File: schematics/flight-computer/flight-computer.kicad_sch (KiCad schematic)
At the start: 45 parts, among them J1 BATT, J2 CHG, J3 SWD, J4 BLACKBOX, J5 USB C, J6 GPS, J7 TELEM, J9 Expansion Slot, U1 MAX14787E, U2 STM32F405RGT6, Y1 26M

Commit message: Rename to Lychee
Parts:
- C1, C10, C11, C12, C2, C3, C4, C5, C6, C7, C8, C9: footprint Strix:C_0402 -> Lychee:C_0402
- D1, D10, D11, D12, D13, D14, D2, D3, D4, D5, D6, D7, D8, D9: footprint Strix:D_0402 -> Lychee:D_0402
- H1, H2, H3, H4: footprint Strix:MountingHole_Pad -> Lychee:MountingHole_Pad
- J1: footprint Strix:Molex_Nano-Fit_105313-1103 -> Lychee:Molex_Nano-Fit_105313-1103
- J2: footprint Strix:Molex_Nano-Fit_105313-1102 -> Lychee:Molex_Nano-Fit_105313-1102
- J3: footprint Strix:Header_SWD -> Lychee:Header_SWD
- J4: footprint Strix:Molex_Nano-Fit_105314-1108 -> Lychee:Molex_Nano-Fit_105314-1108
- J5: footprint Strix:USB_C -> Lychee:USB_C
- J6, J7: footprint Strix:SMA-Edge -> Lychee:SMA-Edge
- J9: footprint Strix:Header_RaspberryPi -> Lychee:Header_RaspberryPi
- R1, R2, R3, R4: footprint Strix:R_0402 -> Lychee:R_0402
- U1: footprint Strix:MAX14787E -> Lychee:MAX14787E
- U2: footprint Strix:STM32F405RGT6 -> Lychee:STM32F405RGT6
- Y1: footprint Strix:Xtal-20x16 -> Lychee:Xtal-20x16
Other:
- title: HAB Flight Computer -> Lychee Flight Computer

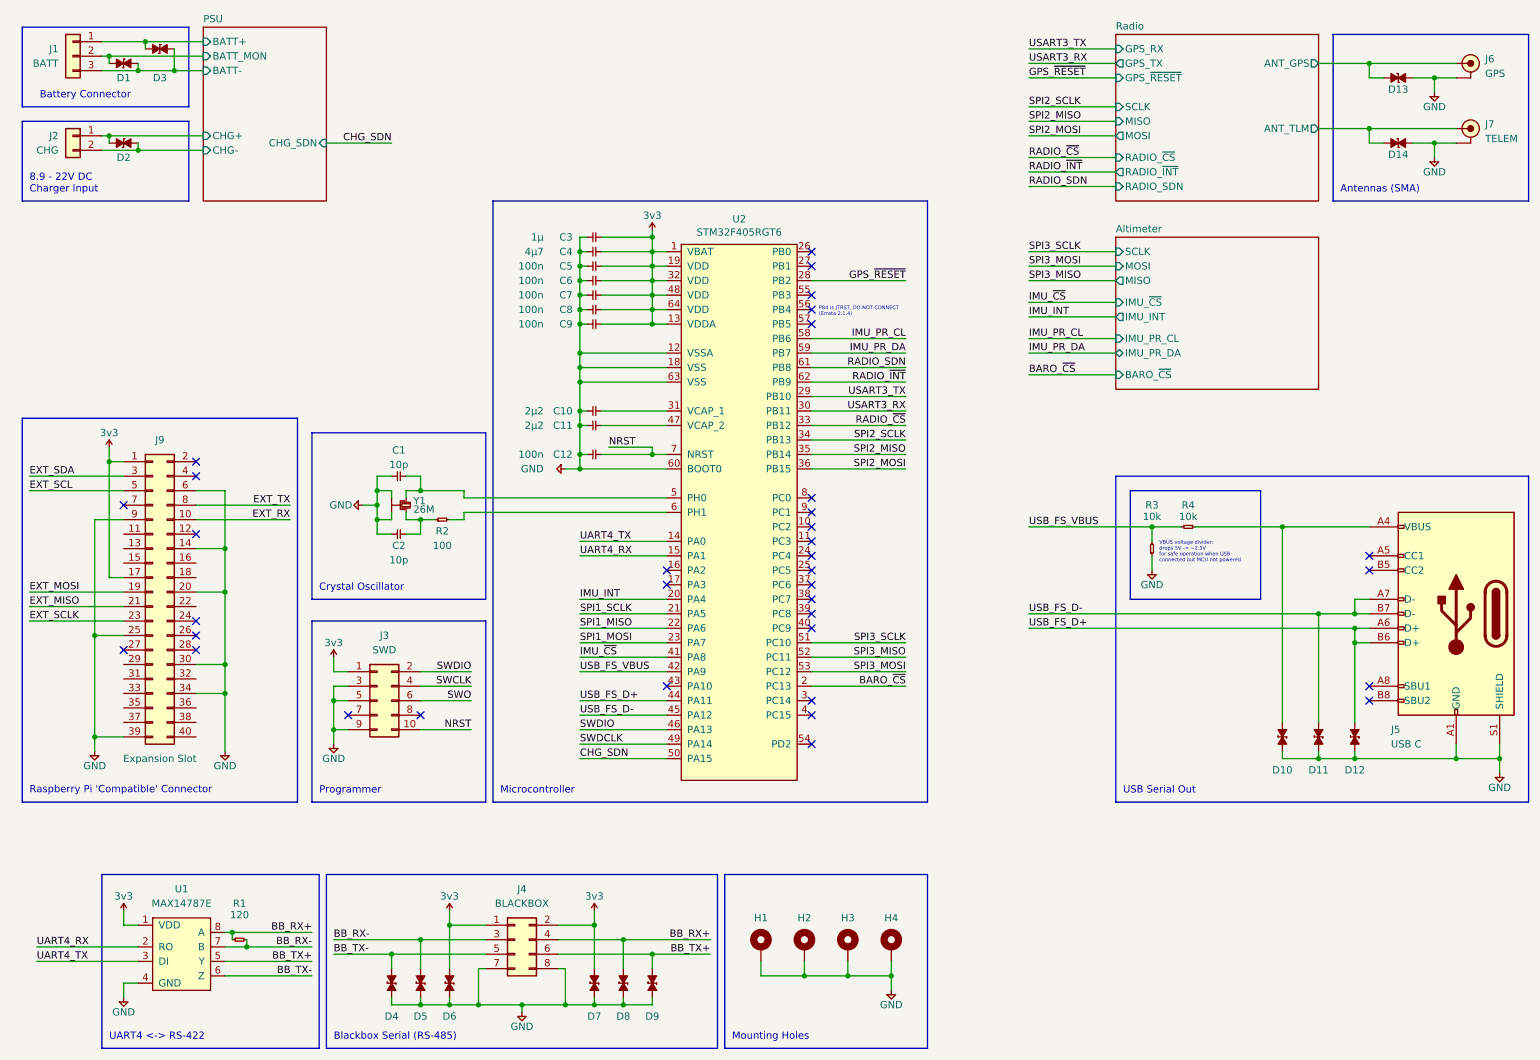
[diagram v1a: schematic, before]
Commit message: Migrate to common Strix lib via submodule
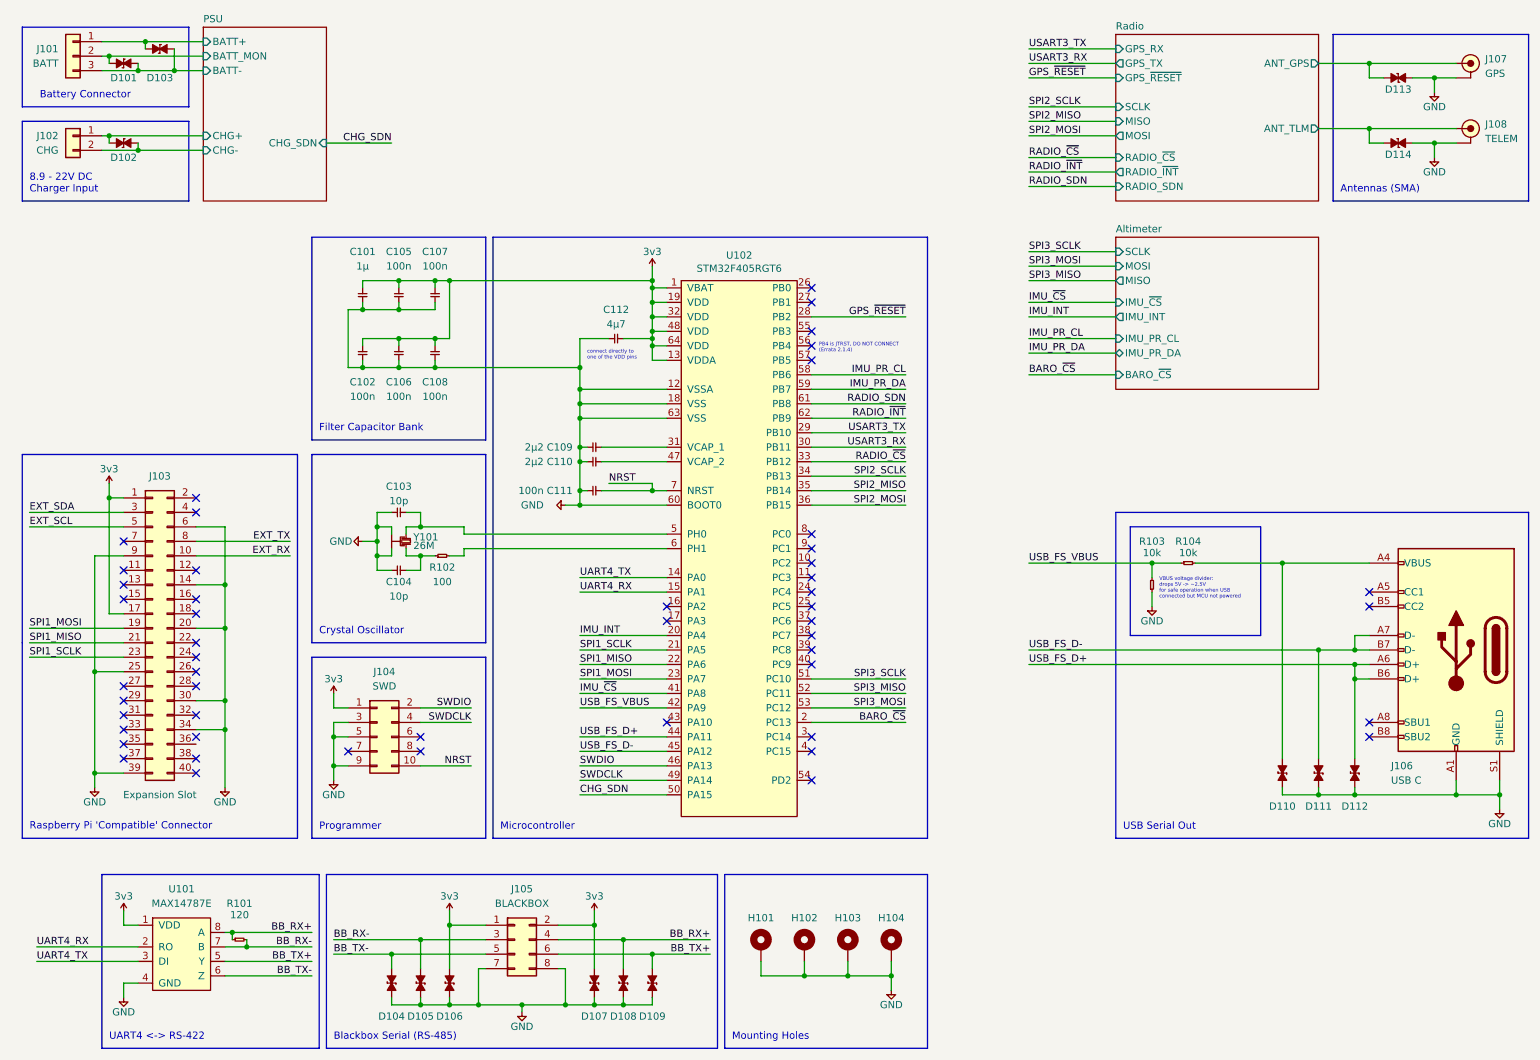
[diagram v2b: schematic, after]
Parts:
- C101: renamed from C3; footprint Lychee:C_0402 -> Strix:C_0402
- C102: renamed from C7; footprint Lychee:C_0402 -> Strix:C_0402
- C103: renamed from C1; footprint Lychee:C_0402 -> Strix:C_0402
- C104: renamed from C2; footprint Lychee:C_0402 -> Strix:C_0402
- C105: renamed from C5; footprint Lychee:C_0402 -> Strix:C_0402
- C106: renamed from C8; footprint Lychee:C_0402 -> Strix:C_0402
- C107: renamed from C6; footprint Lychee:C_0402 -> Strix:C_0402
- C108: renamed from C9; footprint Lychee:C_0402 -> Strix:C_0402
- C109: renamed from C10; footprint Lychee:C_0402 -> Strix:C_0402
- C110: renamed from C11; footprint Lychee:C_0402 -> Strix:C_0402
- C111: renamed from C12; footprint Lychee:C_0402 -> Strix:C_0402
- C112: renamed from C4; footprint Lychee:C_0402 -> Strix:C_0402
- D101: renamed from D1; footprint Lychee:D_0402 -> Strix:D_0402
- D102: renamed from D2; footprint Lychee:D_0402 -> Strix:D_0402
- D103: renamed from D3; footprint Lychee:D_0402 -> Strix:D_0402
- D104: renamed from D4; footprint Lychee:D_0402 -> Strix:D_0402
- D105: renamed from D5; footprint Lychee:D_0402 -> Strix:D_0402
- D106: renamed from D6; footprint Lychee:D_0402 -> Strix:D_0402
- D107: renamed from D7; footprint Lychee:D_0402 -> Strix:D_0402
- D108: renamed from D8; footprint Lychee:D_0402 -> Strix:D_0402
- D109: renamed from D9; footprint Lychee:D_0402 -> Strix:D_0402
- D110: renamed from D10; footprint Lychee:D_0402 -> Strix:D_0402
- D111: renamed from D11; footprint Lychee:D_0402 -> Strix:D_0402
- D112: renamed from D12; footprint Lychee:D_0402 -> Strix:D_0402
- D113: renamed from D13; footprint Lychee:D_0402 -> Strix:D_0402
- D114: renamed from D14; footprint Lychee:D_0402 -> Strix:D_0402
- H101: renamed from H1; footprint Lychee:MountingHole_Pad -> Strix:MountingHole_Pad
- H102: renamed from H2; footprint Lychee:MountingHole_Pad -> Strix:MountingHole_Pad
- H103: renamed from H3; footprint Lychee:MountingHole_Pad -> Strix:MountingHole_Pad
- H104: renamed from H4; footprint Lychee:MountingHole_Pad -> Strix:MountingHole_Pad
- J101: renamed from J1; footprint Lychee:Molex_Nano-Fit_105313-1103 -> Strix:Molex_Nano-Fit_105313-1103
- J102: renamed from J2; footprint Lychee:Molex_Nano-Fit_105313-1102 -> Strix:Molex_Nano-Fit_105313-1102
- J103: renamed from J9; footprint Lychee:Header_RaspberryPi -> Strix:Header_RaspberryPi
- J104: renamed from J3; footprint Lychee:Header_SWD -> Strix:Header_SWD
- J105: renamed from J4; footprint Lychee:Molex_Nano-Fit_105314-1108 -> Strix:Molex_Nano-Fit_105314-1108
- J106: renamed from J5; footprint Lychee:USB_C -> Strix:USB_C
- J107: renamed from J6; footprint Lychee:SMA-Edge -> Strix:SMA-Edge
- J108: renamed from J7; footprint Lychee:SMA-Edge -> Strix:SMA-Edge
- R101: renamed from R1; footprint Lychee:R_0402 -> Strix:R_0402
- R102: renamed from R2; footprint Lychee:R_0402 -> Strix:R_0402
- R103: renamed from R3; footprint Lychee:R_0402 -> Strix:R_0402
- R104: renamed from R4; footprint Lychee:R_0402 -> Strix:R_0402
- U101: renamed from U1; footprint Lychee:MAX14787E -> Strix:MAX14787E
- U102: renamed from U2; footprint Lychee:STM32F405RGT6 -> Strix:STM32F405RGT6
- Y101: renamed from Y1; footprint Lychee:Xtal-20x16 -> Strix:Xtal-20x16
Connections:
- net EXT_MISO is gone; now on net SPI1_MISO: J103.21 (Pin_21)
- net EXT_MOSI is gone; now on net SPI1_MOSI: J103.19 (Pin_19)
- net EXT_SCLK is gone; now on net SPI1_SCLK: J103.23 (Pin_23)
- net SWCLK is gone; now on net SWDCLK: J104.4 (Pin_4)
- net SWO: no longer names the net of J104.6 (Pin_6)
- no-connect marks 35 -> 51
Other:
- note added: "Filter Capacitor Bank"
- note added: "connect directly to one of the VDD pins"
- moved on the sheet: C101, C102, C103, C104, C105, C106, C107, C108, C109, C110, C111, C112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

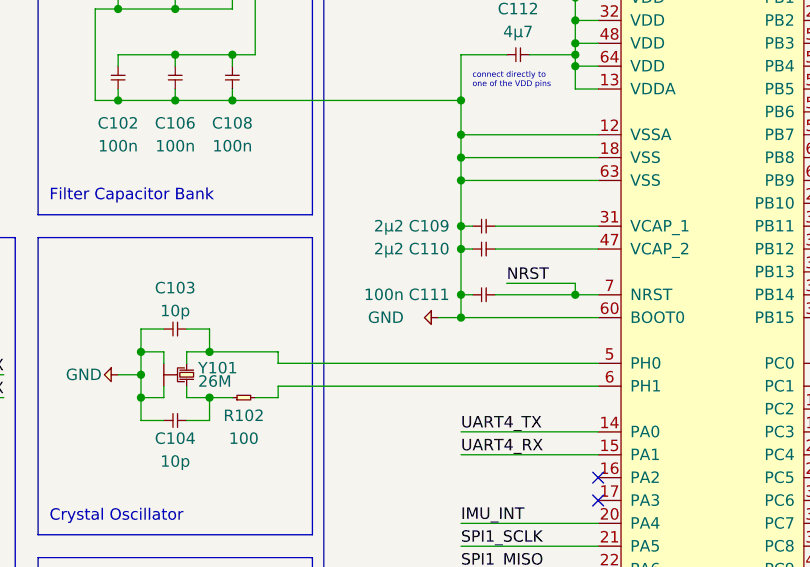
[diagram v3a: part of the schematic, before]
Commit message: Route oscillator
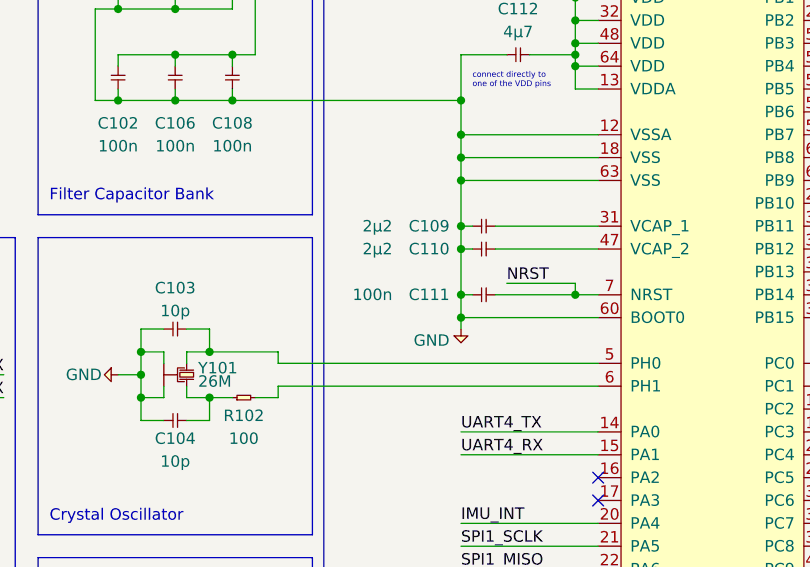
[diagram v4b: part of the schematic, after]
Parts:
- Y101: footprint Strix:Xtal-20x16 -> Strix:Xtal_SMD_2016
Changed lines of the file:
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@@
   (junction (at 86.36 177.8) (diameter 0) (color 0 0 0 0)
   )
-  (junction (at 114.3 101.6) (diameter 0) (color 0 0 0 0)
-  )
   (junction (at 127 62.23) (diameter 0) (color 0 0 0 0)
   )
@@
   (junction (at 114.3 77.47) (diameter 0) (color 0 0 0 0)
   )
+  (junction (at 114.3 101.6) (diameter 0) (color 0 0 0 0)
+  )
   (junction (at 86.36 110.49) (diameter 0) (color 0 0 0 0)
   )
@@
     (stroke (width 0) (type default) (color 0 0 0 0))
   )
-  (wire (pts (xy 111.76 101.6) (xy 114.3 101.6))
-    (stroke (width 0) (type default) (color 0 0 0 0))
-  )
   (polyline (pts (xy 280.67 19.05) (xy 246.38 19.05))
     (stroke (width 0) (type default) (color 0 0 0 0))
@@
     (stroke (width 0) (type default) (color 0 0 0 0))
   )
+  (wire (pts (xy 114.3 101.6) (xy 114.3 102.87))
+    (stroke (width 0) (type default) (color 0 0 0 0))
+  )
   (wire (pts (xy 76.2 77.47) (xy 73.66 77.47))
     (stroke (width 0) (type default) (color 0 0 0 0))
@@
       (effects (font (size 1.27 1.27)) (justify right))
     )
-    (property "Value" "2µ2" (id 1) (at 107.95 91.44 0)
+    (property "Value" "2µ2" (id 1) (at 106.68 91.44 0)
       (effects (font (size 1.27 1.27)) (justify right))
     )
@@
       (effects (font (size 1.27 1.27)) (justify right))
     )
-    (property "Value" "2µ2" (id 1) (at 107.95 93.98 0)
+    (property "Value" "2µ2" (id 1) (at 106.68 93.98 0)
       (effects (font (size 1.27 1.27)) (justify right))
     )
@@
       (effects (font (size 1.27 1.27)) (justify right))
     )
-    (property "Value" "100n" (id 1) (at 107.95 99.06 0)
+    (property "Value" "100n" (id 1) (at 106.68 99.06 0)
       (effects (font (size 1.27 1.27)) (justify right))
     )
@@
     (pin "2")
   )
-  (symbol (lib_id "Strix:GND") (at 111.76 101.6 270) (unit 1)
+  (symbol (lib_id "Strix:GND") (at 114.3 102.87 0) (unit 1)
     (in_bom yes) (on_board yes)
-    (property "Reference" "#PWR0111" (id 0) (at 112.776 98.298 0)
+    (property "Reference" "#PWR0111" (id 0) (at 110.998 101.854 0)
       (effects (font (size 1.27 1.27)) (justify left) hide)
     )
-    (property "Value" "GND" (id 1) (at 107.95 101.6 90)
+    (property "Value" "GND" (id 1) (at 113.03 104.14 0)
       (effects (font (size 1.27 1.27)) (justify right))
     )
-    (property "Footprint" "" (id 2) (at 111.76 101.6 0))
-    (property "Datasheet" "" (id 3) (at 111.76 101.6 0))
+    (property "Footprint" "" (id 2) (at 114.3 102.87 0))
+    (property "Datasheet" "" (id 3) (at 114.3 102.87 0))
     (pin "1")
   )
@@
       (effects (font (size 1.27 1.27)) (justify left top))
     )
-    (property "Footprint" "Strix:Xtal-20x16" (id 2) (at 78.232 107.95 0)
+    (property "Footprint" "Strix:Xtal_SMD_2016" (id 2) (at 78.232 107.95 0)
       (effects (font (size 1.27 1.27)) hide)
     )
@@
     )
     (path "/96d64ec3-74dd-45f3-9f77-b1b10a62a585"
-      (reference "Y101") (unit 1) (value "26M") (footprint "Strix:Xtal-20x16")
+      (reference "Y101") (unit 1) (value "26M") (footprint "Strix:Xtal_SMD_2016")
     )
     (path "/00000000-0000-0000-0000-0000611291b2/f4f237e8-d7a6-465e-996a-94072554fcb5"

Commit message: Change peripheral interface assignments to match layout
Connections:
- net EXT_RX is gone; now on net UART4_RX: J103.10 (Pin_10)
- net EXT_TX is gone; now on net UART4_TX: J103.8 (Pin_8)
- net IMU_PR_CL is gone; now on net I2C1_SCL: U102.58 (PB6)
- net IMU_PR_DA is gone; now on net I2C1_SDA: U102.59 (PB7)
- net GPS_~{RESET}: now also U102.25 (PC5); no longer U102.28 (PB2)
- net IMU_INT: now also U102.24 (PC4); no longer U102.20 (PA4)
- net IMU_~{CS}: now also U102.43 (PA10); no longer U102.41 (PA8)
- net SPI1_MISO: no longer J103.21 (Pin_21)
- net SPI1_MOSI: no longer J103.19 (Pin_19)
- net SPI1_SCLK: no longer J103.23 (Pin_23)
- net SPI3_MISO: now also J103.21 (Pin_21)
- net SPI3_MOSI: now also J103.19 (Pin_19)
- net SPI3_SCLK: now also J103.23 (Pin_23)
- net UART4_RX: no longer U101.2 (RO)
- net UART4_TX: no longer U101.3 (DI)
- net USART3_RX: now also U101.2 (RO)
- net USART3_TX: now also U101.3 (DI)
- net USART2_TX: now reaches U102.16 (PA2)
- net USART2_RX: now reaches U102.17 (PA3)
- net I2C3_SDA: now reaches U102.40 (PC9)
- net EXT_SCL renamed I2C1_SCL
- net EXT_SDA renamed I2C1_SDA
- new net I2C3_SCL: U102.41 (PA8)
- no-connect marks 51 -> 47

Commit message: Route GPIO peripheral connections
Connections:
- net BARO_~{CS}: now also U102.20 (PA4); no longer U102.2 (PC13)
- net CHG_SDN: now also U102.11 (PC3); no longer U102.50 (PA15)
- net IMU_~{CS}: now also U102.26 (PB0); no longer U102.43 (PA10)
- net RADIO_SDN: now also U102.38 (PC7); no longer U102.61 (PB8)
- net RADIO_~{INT}: now also U102.37 (PC6); no longer U102.62 (PB9)
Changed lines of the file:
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@@
   (no_connect (at 154.94 76.2))
   (no_connect (at 154.94 73.66))
-  (no_connect (at 154.94 124.46))
+  (no_connect (at 154.94 83.82))
   (no_connect (at 154.94 144.78))
-  (no_connect (at 154.94 63.5))
+  (no_connect (at 129.54 139.7))
   (no_connect (at 154.94 66.04))
   (no_connect (at 252.73 142.24))
-  (no_connect (at 129.54 124.46))
+  (no_connect (at 154.94 139.7))
   (no_connect (at 154.94 142.24))
   (no_connect (at 86.36 144.78))
@@
   (no_connect (at 154.94 68.58))
   (no_connect (at 154.94 149.86))
-  (no_connect (at 154.94 121.92))
+  (no_connect (at 154.94 86.36))
   (no_connect (at 46.99 113.03))
   (no_connect (at 46.99 133.35))
@@
   (no_connect (at 154.94 111.76))
   (no_connect (at 154.94 127))
-  (no_connect (at 154.94 114.3))
+  (no_connect (at 129.54 152.4))
   (no_connect (at 46.99 125.73))
   (no_connect (at 34.29 135.89))
@@
     (stroke (width 0) (type default) (color 0 0 0 0))
   )
-  (wire (pts (xy 154.94 86.36) (xy 171.45 86.36))
+  (wire (pts (xy 154.94 121.92) (xy 171.45 121.92))
     (stroke (width 0) (type default) (color 0 0 0 0))
   )
@@
     (stroke (width 0) (type default) (color 0 0 0 0))
   )
-  (wire (pts (xy 114.3 139.7) (xy 129.54 139.7))
+  (wire (pts (xy 171.45 63.5) (xy 154.94 63.5))
     (stroke (width 0) (type default) (color 0 0 0 0))
   )
@@
     (stroke (width 0) (type default) (color 0 0 0 0))
   )
-  (wire (pts (xy 114.3 152.4) (xy 129.54 152.4))
+  (wire (pts (xy 171.45 114.3) (xy 154.94 114.3))
     (stroke (width 0) (type default) (color 0 0 0 0))
   )
@@
     (stroke (width 0) (type default) (color 0 0 0 0))
   )
-  (wire (pts (xy 171.45 83.82) (xy 154.94 83.82))
+  (wire (pts (xy 171.45 124.46) (xy 154.94 124.46))
     (stroke (width 0) (type default) (color 0 0 0 0))
   )
@@
     (stroke (width 0) (type default) (color 0 0 0 0))
   )
-  (wire (pts (xy 154.94 139.7) (xy 171.45 139.7))
+  (wire (pts (xy 129.54 124.46) (xy 114.3 124.46))
     (stroke (width 0) (type default) (color 0 0 0 0))
   )
@@
     (effects (font (size 1.27 1.27)) (justify left bottom))
   )
-  (label "BARO_~{CS}" (at 171.45 139.7 180)
-    (effects (font (size 1.27 1.27)) (justify right bottom))
+  (label "BARO_~{CS}" (at 114.3 124.46 0)
+    (effects (font (size 1.27 1.27)) (justify left bottom))
   )
   (label "SPI2_MISO" (at 193.04 34.29 0)
@@
     (effects (font (size 1.27 1.27)) (justify left bottom))
   )
-  (label "RADIO_~{INT}" (at 171.45 86.36 180)
+  (label "RADIO_~{INT}" (at 171.45 121.92 180)
     (effects (font (size 1.27 1.27)) (justify right bottom))
   )
@@
     (effects (font (size 1.27 1.27)) (justify left bottom))
   )
-  (label "CHG_SDN" (at 114.3 152.4 0)
-    (effects (font (size 1.27 1.27)) (justify left bottom))
+  (label "CHG_SDN" (at 171.45 114.3 180)
+    (effects (font (size 1.27 1.27)) (justify right bottom))
   )
   (label "I2C1_SDA" (at 17.78 102.87 0)
@@
     (effects (font (size 1.27 1.27)) (justify left bottom))
   )
-  (label "IMU_~{CS}" (at 114.3 139.7 0)
-    (effects (font (size 1.27 1.27)) (justify left bottom))
+  (label "IMU_~{CS}" (at 171.45 63.5 180)
+    (effects (font (size 1.27 1.27)) (justify right bottom))
   )
   (label "RADIO_~{CS}" (at 193.04 40.64 0)
@@
     (effects (font (size 1.27 1.27)) (justify left bottom))
   )
-  (label "RADIO_SDN" (at 171.45 83.82 180)
-    (effects (font (size 1.27 1.27)) (justify right bottom))
-  )
+  (label "RADIO_SDN" (at 171.45 124.46 180)
+    (effects (font (size 1.27 1.27)) (justify right bottom))
+  )

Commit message: Complete first draft
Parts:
- removed D102: D_ESD, Strix:D_0402, symbol Strix:D_ESD
- removed J102: CHG, Strix:Molex_Nano-Fit_105313-1102, symbol Strix:Conn_01x02
- C111: renamed from C103; Farnell (none) -> 2494183
- C112: renamed from C104; Farnell (none) -> 2494183
- J105: renamed from J106; Farnell 2990003 -> 2990510
- J107: renamed from J105; RS (none) -> 162-3692
- R101: renamed from R102; Farnell (none) -> 2447095
- R102: renamed from R104; Farnell (none) -> 2447096
- R103: Farnell (none) -> 2447096
- R104: renamed from R101; Farnell (none) -> 2447103
- renumbered C105 to C102, C107 to C103, C112 to C104, C102 to C105, C108 to C107, C109 to C108, C110 to C109, C111 to C110, D103 to D101, D101 to D102, D113 to D103, D114 to D104, D110 to D105, D111 to D106, D112 to D107, D104 to D108, D105 to D109, D106 to D110, D107 to D111, D108 to D112, D109 to D113, J107 to J102, J108 to J103, J103 to J104, J104 to J106, U102 to U101, U101 to U102
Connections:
- net CHG_SDN: no longer names the net of U101.11 (PC3)
- no-connect marks 47 -> 48
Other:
- sheet PSU ports: added none; removed CHG+, CHG-, CHG_SDN
- note removed: "8.9 - 22V DC Charger Input"
